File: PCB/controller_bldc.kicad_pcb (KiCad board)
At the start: 2 copper layers, 210 x 125 mm, 72 parts, among them J1 Battery Supply, J2 Conn_01x11_Male, J6 LM35, J7 Hall Sensors, J9 BLDC Motor, K1 RAYEX-L90B, Q1 IRF1010N, Q2 IRF1010N, Q3 IRF1010N, Q4 IRF1010N, Q5 IRF1010N, Q6 IRF1010N, Q7 PN2222A, SW1 ON_OFF, U1 ESP32-DEVKITC-32D, U2 MC1458P, U3 LM2596SOURCE_Pin2, U4 IR2103, U5 LM2596SOURCE, U8 IR2103, U9 IR2103

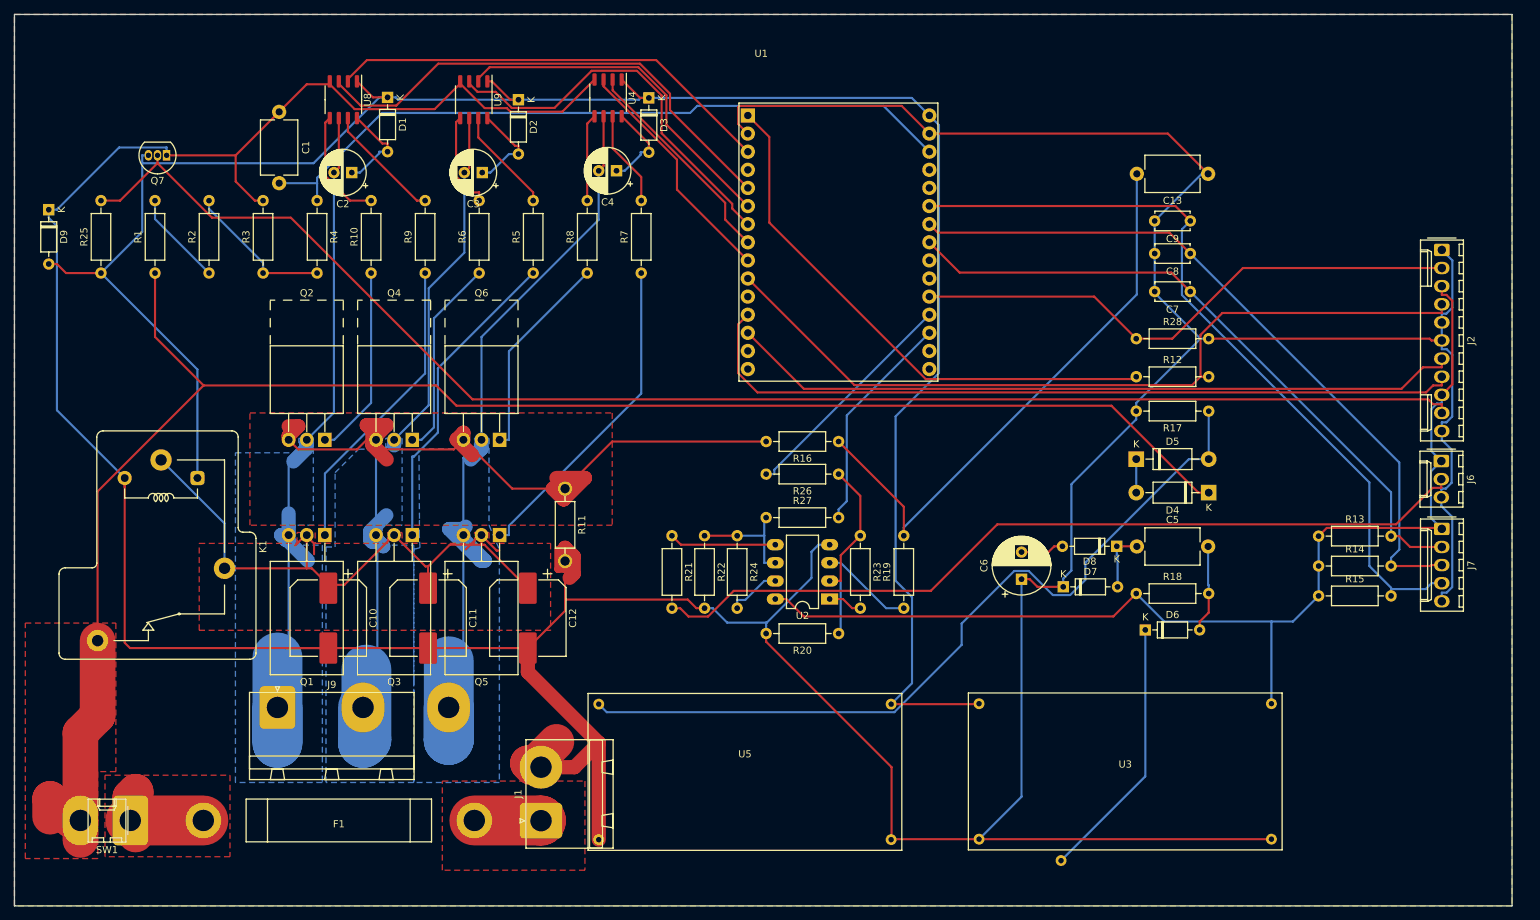
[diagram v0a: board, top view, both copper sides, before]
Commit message: PCB v1.1 with the res. for throttle
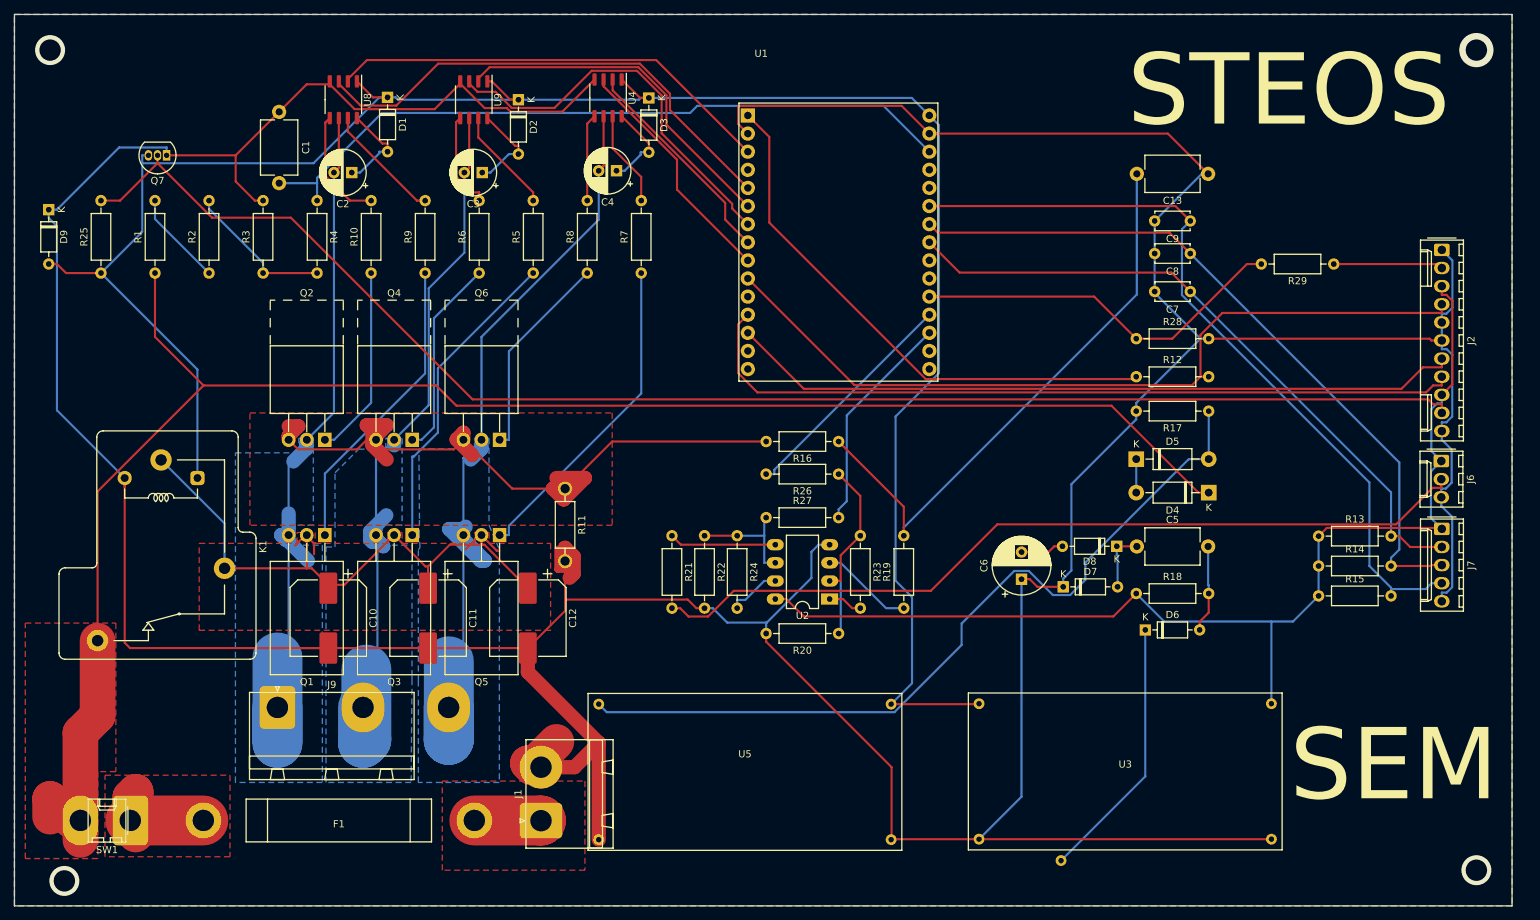
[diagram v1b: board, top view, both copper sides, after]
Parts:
- added R29: 2.5k, Resistor_THT:R_Axial_DIN0207_L6.3mm_D2.5mm_P10.16mm_Horizontal, F.Cu at (185.0, 35.0)
- R24: value 150k -> 75k
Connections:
- net Net-(C6-Pad2) renamed -5V
- J2 pad 2: Throttle -> Throttle_Raw
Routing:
- net Throttle: track 78.4 -> 53.3 mm
- net Throttle_Raw: track 0.00 -> 15.4 mm
- net GND: vias 0 -> 4
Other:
- board text added: "SEM"
- board text added: "STEOS"

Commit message: To be reviewed by Yahico PCB
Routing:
- net GND: track 727.3 -> 719.9 mm

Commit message: Before freerouting
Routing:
- net GND: track 719.9 -> 53.1 mm, vias 4 -> 0
- net +12V: track 293.1 -> 0.00 mm
- net +36V: track 244.7 -> 36.9 mm
- net OPC_1: track 206.5 -> 0.00 mm
- net +5V: track 157.8 -> 0.00 mm
- net LM35-RAW: track 117.1 -> 0.00 mm
- net Brake: track 113.5 -> 0.00 mm
- net Net-(D5-Pad2): track 113.4 -> 0.00 mm
- net TX-LCD: track 110.2 -> 0.00 mm
- net HALL-C: track 110.1 -> 0.00 mm
- net Current_Sensor: track 107.5 -> 0.00 mm
- net RX-LCD: track 103.0 -> 0.00 mm
- net HALL-B: track 101.9 -> 0.00 mm
- net Voltage_Sensor: track 101.2 -> 0.00 mm
- net HALL-A: track 93.2 -> 0.00 mm
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- removed copper zone on B.Cu, net GND
- removed copper zone on F.Cu, net GND

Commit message: Sento to Yahiko
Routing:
- net GND: track 53.1 -> 692.3 mm, vias 0 -> 4
- net +12V: track 0.00 -> 315.3 mm
- net OPC_1: track 0.00 -> 214.1 mm
- net +36V: track 36.9 -> 244.4 mm
- net +5V: track 0.00 -> 161.2 mm
- net LM35-RAW: track 0.00 -> 116.8 mm
- net HALL-C: track 0.00 -> 113.7 mm
- net TX-LCD: track 0.00 -> 113.3 mm
- net Net-(D5-Pad2): track 0.00 -> 109.6 mm
- net Brake: track 0.00 -> 108.5 mm
- net HALL-B: track 0.00 -> 108.4 mm
- net Voltage_Sensor: track 0.00 -> 106.9 mm
- net RX-LCD: track 0.00 -> 104.2 mm
- net HALL-A: track 0.00 -> 93.2 mm
- net Current_Sensor_AO: track 0.00 -> 81.3 mm
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- added copper zone on B.Cu, net GND
- added copper zone on F.Cu, net GND
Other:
- net class Default: clearance 0.2 -> 0.5
- rule trace_clearance: 0.2 -> 0.5
